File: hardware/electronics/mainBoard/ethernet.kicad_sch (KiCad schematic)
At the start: 34 parts, among them J4 MRJ-5381-01, U4 LAN8742AI

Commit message: assigned net classes
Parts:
- renumbered C39 to C36, C36 to C37, C37 to C38, C38 to C39, R26 to R15, R27 to R16, R28 to R17, R29 to R18, R18 to R19, R22 to R21, R23 to R22, R24 to R23, R15 to R24, R16 to R25, R17 to R26, R19 to R27, R25 to R28, R21 to R29
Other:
- note added: "RMII: 50MHz clock MII: 25MHz clock"
- note added: "Single ended impedance: 50 Ohm Length matching: +/- 1.27mm for RX/RX and TX/TX pairs"

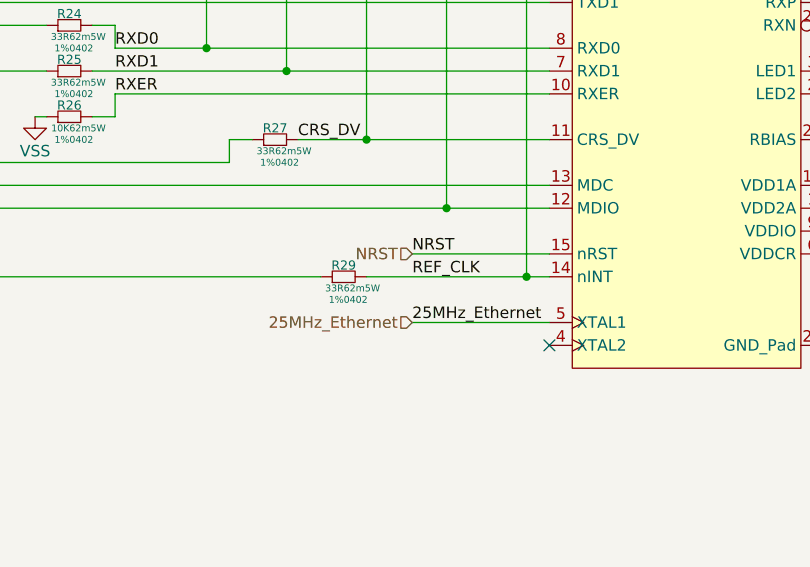
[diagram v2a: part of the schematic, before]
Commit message: fixed net names
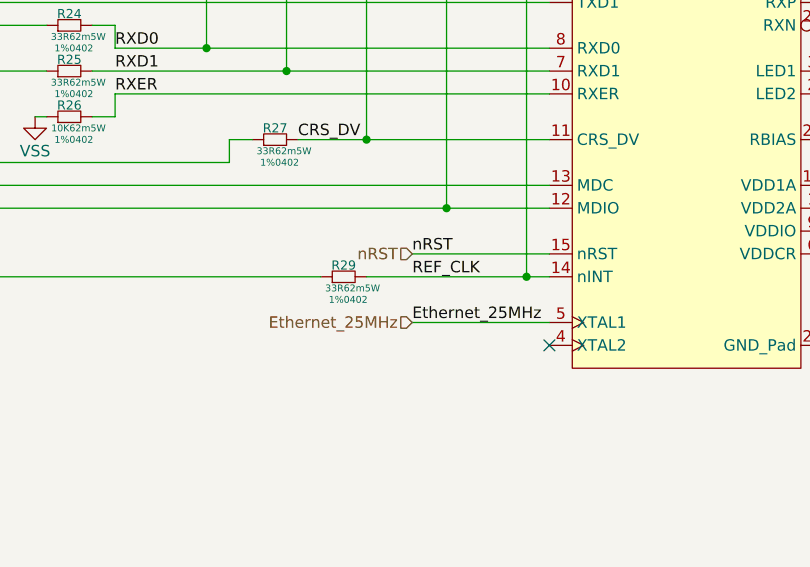
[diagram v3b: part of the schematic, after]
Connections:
- net 25MHz_Ethernet renamed Ethernet_25MHz
- net NRST renamed nRST
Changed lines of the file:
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@@
 		)
 	)
-	(label "25MHz_Ethernet"
+	(label "Ethernet_25MHz"
 		(at 109.22 133.35 0)
 		(effects
@@
 		)
 	)
-	(label "NRST"
+	(label "nRST"
 		(at 109.22 125.73 0)
 		(effects
@@
 		)
 	)
-	(hierarchical_label "25MHz_Ethernet"
+	(hierarchical_label "Ethernet_25MHz"
 		(shape input)
 		(at 109.22 133.35 180)
@@
 		)
 	)
-	(hierarchical_label "NRST"
+	(hierarchical_label "nRST"
 		(shape input)
 		(at 109.22 125.73 180)

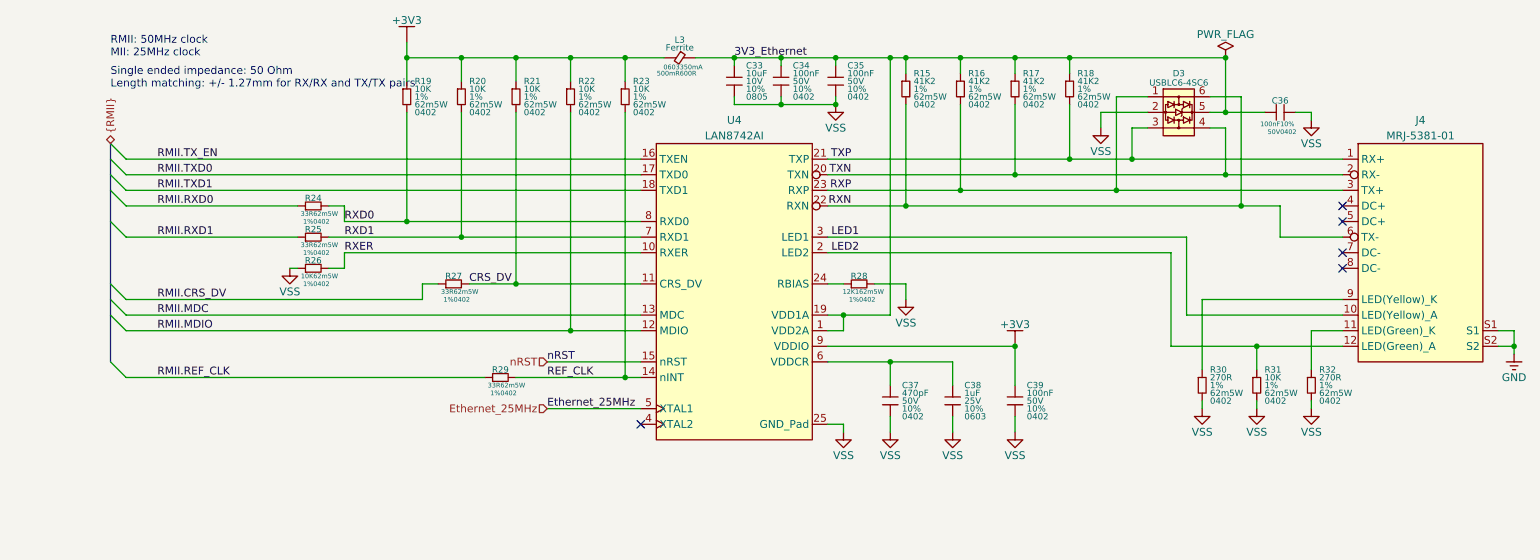
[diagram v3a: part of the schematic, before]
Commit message: fixed net names and added notes
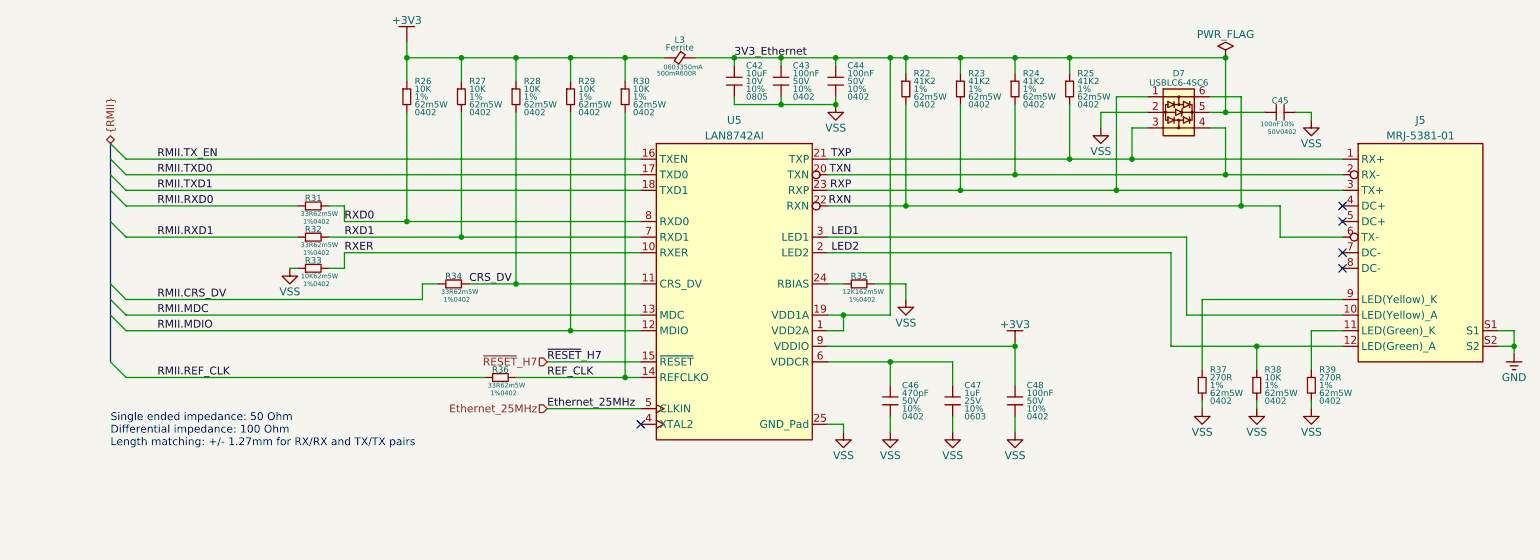
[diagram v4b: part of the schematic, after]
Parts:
- renumbered C33 to C42, C34 to C43, C35 to C44, C36 to C45, C37 to C46, C38 to C47, C39 to C48, D3 to D7, J4 to J5, R15 to R22, R16 to R23, R17 to R24, R18 to R25, R19 to R26, R20 to R27, R21 to R28, R22 to R29, R23 to R30, R24 to R31, R25 to R32, R26 to R33, R27 to R34, R28 to R35, R29 to R36, R30 to R37, R31 to R38, R32 to R39, U4 to U5
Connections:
- net nRST renamed ~{RESET}_H7
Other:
- note added: "Single ended impedance: 50 Ohm Differential impedance: 100 Ohm Length matching: +/- 1.27mm for RX/RX and TX/TX pairs"
- note removed: "RMII: 50MHz clock MII: 25MHz clock"
- note removed: "Single ended impedance: 50 Ohm Length matching: +/- 1.27mm for RX/RX and TX/TX pairs"

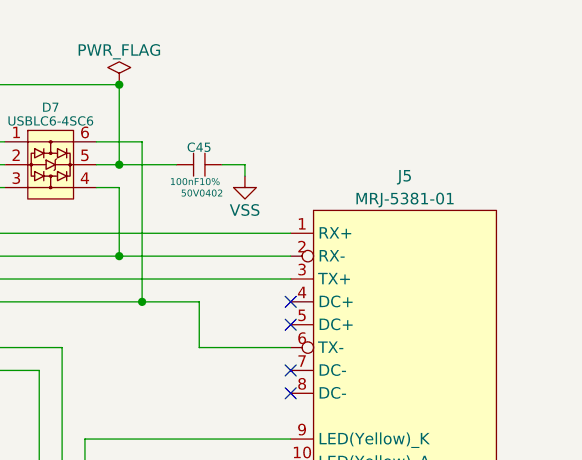
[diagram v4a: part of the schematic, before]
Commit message: renumber references
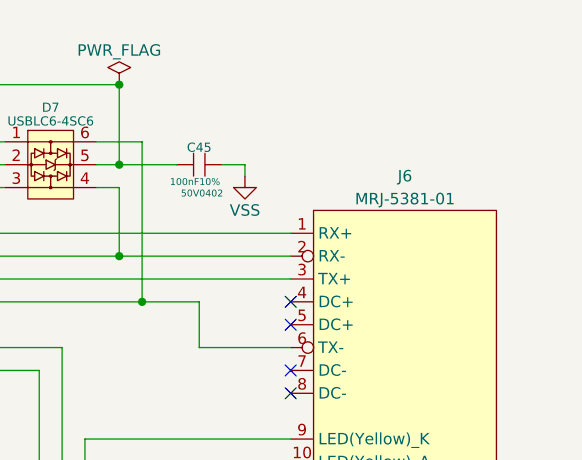
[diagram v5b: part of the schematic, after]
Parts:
- renumbered J5 to J6
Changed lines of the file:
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@@
 		(dnp no)
 		(fields_autoplaced yes)
-		(property "Reference" "#PWR0114"
+		(property "Reference" "#PWR0116"
 			(at 233.68 133.35 0)
 			(effects
@@
 			(project "mainBoard"
 				(path "/be16e32f-2ccf-4272-9ec7-94d5fe7a55e0/7b4a835f-742a-4147-9d08-db52b169b2a7"
-					(reference "#PWR0114")
+					(reference "#PWR0116")
 					(unit 1)
 				)
@@
 		(dnp no)
 		(fields_autoplaced yes)
-		(property "Reference" "#PWR0112"
+		(property "Reference" "#PWR0114"
 			(at 215.9 133.35 0)
 			(effects
@@
 			(project "mainBoard"
 				(path "/be16e32f-2ccf-4272-9ec7-94d5fe7a55e0/7b4a835f-742a-4147-9d08-db52b169b2a7"
-					(reference "#PWR0112")
+					(reference "#PWR0114")
 					(unit 1)
 				)
@@
 		(dnp no)
 		(fields_autoplaced yes)
-		(property "Reference" "#PWR0113"
+		(property "Reference" "#PWR0115"
 			(at 224.79 133.35 0)
 			(effects
@@
 			(project "mainBoard"
 				(path "/be16e32f-2ccf-4272-9ec7-94d5fe7a55e0/7b4a835f-742a-4147-9d08-db52b169b2a7"
-					(reference "#PWR0113")
+					(reference "#PWR0115")
 					(unit 1)
 				)
@@
 		(dnp no)
 		(fields_autoplaced yes)
-		(property "Reference" "J5"
+		(property "Reference" "J6"
 			(at 251.46 86.36 0)
 			(do_not_autoplace yes)
@@
 			(project "mainBoard"
 				(path "/be16e32f-2ccf-4272-9ec7-94d5fe7a55e0/7b4a835f-742a-4147-9d08-db52b169b2a7"
-					(reference "J5")
+					(reference "J6")
 					(unit 1)
 				)
@@
 		(dnp no)
 		(fields_autoplaced yes)
-		(property "Reference" "#PWR0109"
+		(property "Reference" "#PWR0111"
 			(at 167.64 115.57 0)
 			(effects
@@
 			(project "mainBoard"
 				(path "/be16e32f-2ccf-4272-9ec7-94d5fe7a55e0/7b4a835f-742a-4147-9d08-db52b169b2a7"
-					(reference "#PWR0109")
+					(reference "#PWR0111")
 					(unit 1)
 				)
@@
 		(dnp no)
 		(fields_autoplaced yes)
-		(property "Reference" "#PWR0104"
+		(property "Reference" "#PWR0106"
 			(at 86.36 73.66 0)
 			(effects
@@
 			(project "mainBoard"
 				(path "/be16e32f-2ccf-4272-9ec7-94d5fe7a55e0/7b4a835f-742a-4147-9d08-db52b169b2a7"
-					(reference "#PWR0104")
+					(reference "#PWR0106")
 					(unit 1)
 				)
@@
 		(dnp no)
 		(fields_autoplaced yes)
-		(property "Reference" "#PWR0119"
+		(property "Reference" "#PWR0121"
 			(at 30.48 191.77 0)
 			(effects
@@
 			(project "mainBoard"
 				(path "/be16e32f-2ccf-4272-9ec7-94d5fe7a55e0/7b4a835f-742a-4147-9d08-db52b169b2a7"
-					(reference "#PWR0119")
+					(reference "#PWR0121")
 					(unit 1)
 				)
@@
 		(dnp no)
 		(fields_autoplaced yes)
-		(property "Reference" "#PWR0115"
+		(property "Reference" "#PWR0117"
 			(at 157.48 137.16 0)
 			(effects
@@
 			(project "mainBoard"
 				(path "/be16e32f-2ccf-4272-9ec7-94d5fe7a55e0/7b4a835f-742a-4147-9d08-db52b169b2a7"
-					(reference "#PWR0115")
+					(reference "#PWR0117")
 					(unit 1)
 				)
@@
 		(dnp no)
 		(fields_autoplaced yes)
-		(property "Reference" "#PWR0105"
+		(property "Reference" "#PWR0107"
 			(at 156.21 83.82 0)
 			(effects
@@
 			(project "mainBoard"
 				(path "/be16e32f-2ccf-4272-9ec7-94d5fe7a55e0/7b4a835f-742a-4147-9d08-db52b169b2a7"
-					(reference "#PWR0105")
+					(reference "#PWR0107")
 					(unit 1)
 				)
@@
 		(dnp no)
 		(fields_autoplaced yes)
-		(property "Reference" "#PWR0107"
+		(property "Reference" "#PWR0109"
 			(at 199.39 87.63 0)
 			(effects
@@
 			(project "mainBoard"
 				(path "/be16e32f-2ccf-4272-9ec7-94d5fe7a55e0/7b4a835f-742a-4147-9d08-db52b169b2a7"
-					(reference "#PWR0107")
+					(reference "#PWR0109")
 					(unit 1)
 				)
@@
 		(dnp no)
 		(fields_autoplaced yes)
-		(property "Reference" "#PWR0118"
+		(property "Reference" "#PWR0120"
 			(at 185.42 137.16 0)
 			(effects
@@
 			(project "mainBoard"
 				(path "/be16e32f-2ccf-4272-9ec7-94d5fe7a55e0/7b4a835f-742a-4147-9d08-db52b169b2a7"
-					(reference "#PWR0118")
+					(reference "#PWR0120")
 					(unit 1)
 				)
@@
 		(dnp no)
 		(fields_autoplaced yes)
-		(property "Reference" "#PWR0117"
+		(property "Reference" "#PWR0119"
 			(at 175.26 137.16 0)
 			(effects
@@
 			(project "mainBoard"
 				(path "/be16e32f-2ccf-4272-9ec7-94d5fe7a55e0/7b4a835f-742a-4147-9d08-db52b169b2a7"
-					(reference "#PWR0117")
+					(reference "#PWR0119")
 					(unit 1)
 				)
@@
 		(dnp no)
 		(fields_autoplaced yes)
-		(property "Reference" "#PWR0110"
+		(property "Reference" "#PWR0112"
 			(at 185.42 123.19 0)
 			(effects
@@
 			(project "mainBoard"
 				(path "/be16e32f-2ccf-4272-9ec7-94d5fe7a55e0/7b4a835f-742a-4147-9d08-db52b169b2a7"
-					(reference "#PWR0110")
+					(reference "#PWR0112")
 					(unit 1)
 				)
@@
 		(dnp no)
 		(fields_autoplaced yes)
-		(property "Reference" "#PWR0116"
+		(property "Reference" "#PWR0118"
 			(at 165.1 137.16 0)
 			(effects
@@
 			(project "mainBoard"
 				(path "/be16e32f-2ccf-4272-9ec7-94d5fe7a55e0/7b4a835f-742a-4147-9d08-db52b169b2a7"
-					(reference "#PWR0116")
+					(reference "#PWR0118")
 					(unit 1)
 				)
@@
 		(dnp no)
 		(fields_autoplaced yes)
-		(property "Reference" "#PWR0108"
+		(property "Reference" "#PWR0110"
 			(at 67.31 110.49 0)
 			(effects
@@
 			(project "mainBoard"
 				(path "/be16e32f-2ccf-4272-9ec7-94d5fe7a55e0/7b4a835f-742a-4147-9d08-db52b169b2a7"
-					(reference "#PWR0108")
+					(reference "#PWR0110")
 					(unit 1)
 				)
@@
 		(dnp no)
 		(fields_autoplaced yes)
-		(property "Reference" "#PWR0106"
+		(property "Reference" "#PWR0108"
 			(at 233.68 86.36 0)
 			(effects
@@
 			(project "mainBoard"
 				(path "/be16e32f-2ccf-4272-9ec7-94d5fe7a55e0/7b4a835f-742a-4147-9d08-db52b169b2a7"
-					(reference "#PWR0106")
+					(reference "#PWR0108")
 					(unit 1)
 				)
@@
 		(dnp no)
 		(fields_autoplaced yes)
-		(property "Reference" "#PWR0111"
+		(property "Reference" "#PWR0113"
 			(at 266.7 124.46 0)
 			(effects
@@
 			(project ""
 				(path "/be16e32f-2ccf-4272-9ec7-94d5fe7a55e0/7b4a835f-742a-4147-9d08-db52b169b2a7"
-					(reference "#PWR0111")
+					(reference "#PWR0113")
 					(unit 1)
 				)

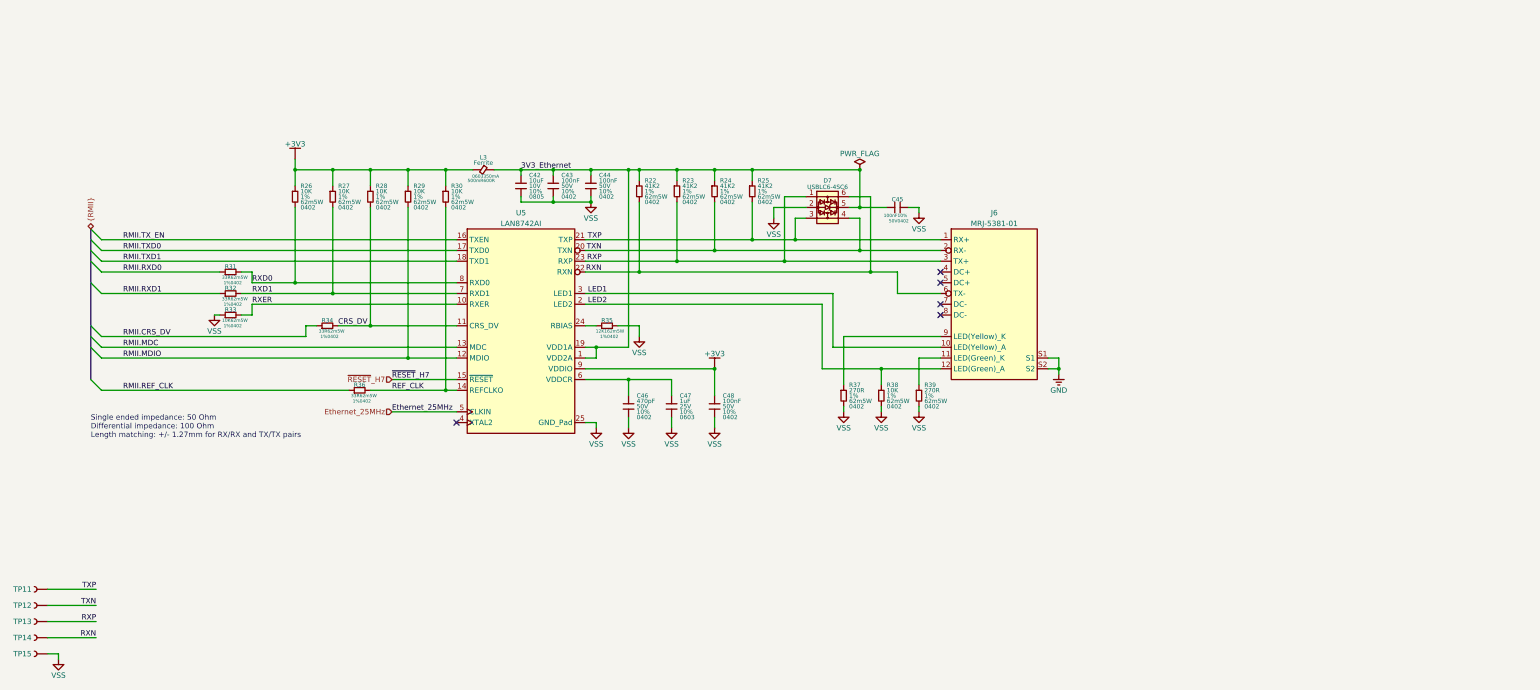
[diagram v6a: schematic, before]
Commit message: added pulse transformer, organized page, and added notes
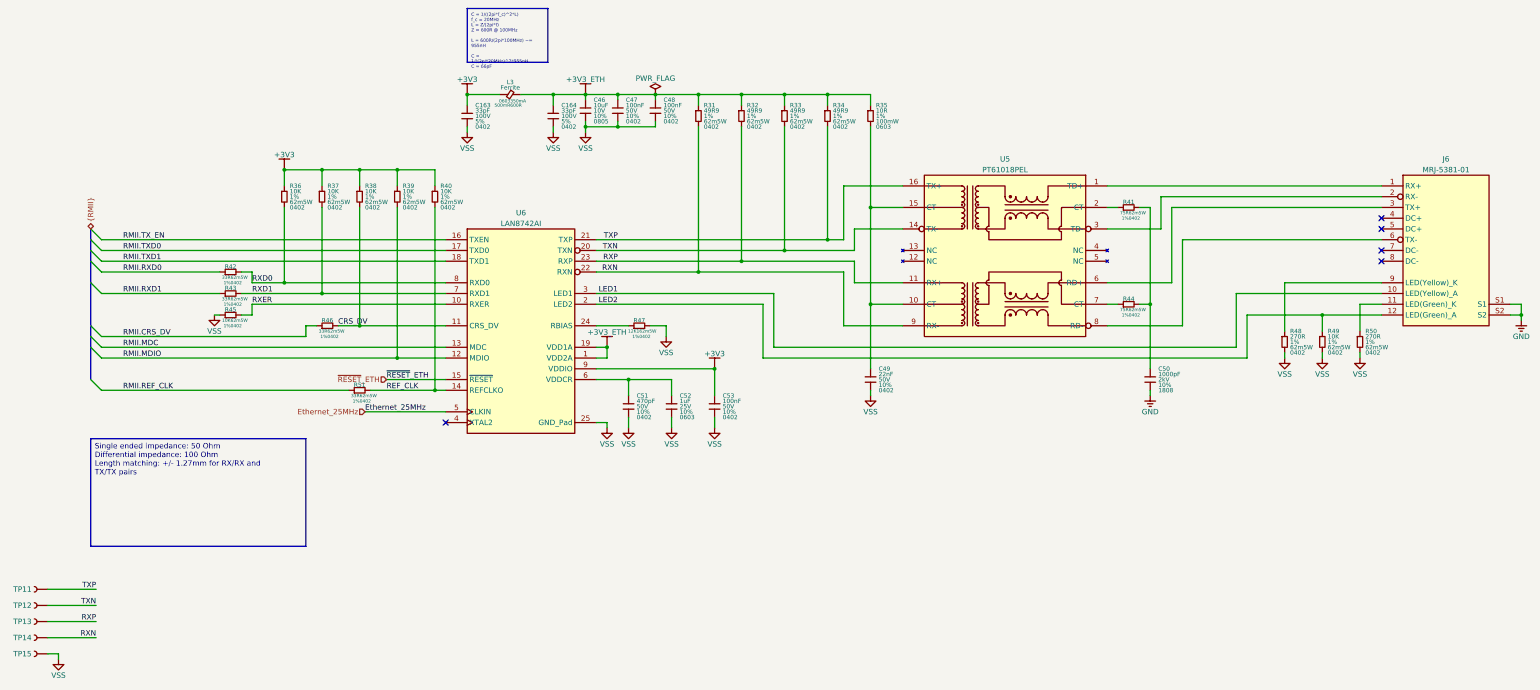
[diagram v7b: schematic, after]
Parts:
- removed C45: 100nF, lib_passives:GCM0402, symbol lib_sch:C_horizontal
- removed D7: USBLC6-4SC6, lib_ICs:SOT2395P280X145-6, symbol lib_sch:D_TVS_2CH_PWR
- removed R22, R23, R24, R25: 41K2, lib_passives:CRCW0402, symbol lib_sch:R
- added C163, C164: 33pF, lib_passives:GCM0402, symbol lib_sch:C
- added C49: 22nF, lib_passives:GCM0402, symbol lib_sch:C
- added C50: 1000pF, lib_passives:GR442, symbol lib_sch:C
- added R31, R32, R33, R34: 49R9, lib_passives:CRCW0402, symbol lib_sch:R
- added R35: 10R, lib_passives:CRCW0603, symbol lib_sch:R
- added R41, R44: 75R, lib_passives:CRCW0402, symbol lib_sch:R_horizontal
- added U5: PT61018PEL, lib_ICs:SOP127P930X565-16, symbol lib_sch:LAN_10/100_Base-T_Pulse_Transformer
- renumbered C42 to C46, C43 to C47, C44 to C48, C46 to C51, C47 to C52, C48 to C53, R26 to R36, R27 to R37, R28 to R38, R29 to R39, R30 to R40, R31 to R42, R32 to R43, R33 to R45, R34 to R46, R35 to R47, R37 to R48, R38 to R49, R39 to R50, R36 to R51, U5 to U6
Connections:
- net +3V3: now also C163.1
- net GND: now also C50.2
- net RXN: now also R31.2, U5.9 (RX-); no longer J6.6 (TX-)
- net RXP: now also R32.2, U5.11 (RX+); no longer J6.3 (TX+)
- net TXN: now also R33.2, U5.14 (TX-); no longer J6.2 (RX-)
- net TXP: now also R34.2, U5.16 (TX+); no longer J6.1 (RX+)
- net VSS: now also C163.2, C164.2, C49.2
- net 3V3_Ethernet renamed +3V3_ETH
- net +3V3_ETH: now also C164.1, R31.1, R32.1, R33.1, R34.1, R35.1
- net ~{RESET}_H7 renamed ~{RESET}_ETH
- new net: J6.1 (RX+), U5.1 (TD+)
- new net: C49.1, R35.2, U5.10 (CT), U5.15 (CT)
- new net: R41.1, U5.2 (CT)
- new net: J6.2 (RX-), U5.3 (TD-)
- new net: J6.3 (TX+), U5.6 (RD+)
- new net: R44.1, U5.7 (CT)
- new net: J6.6 (TX-), U5.8 (RD-)
- new net: C50.1, R41.2, R44.2
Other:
- note removed: "Single ended impedance: 50 Ohm Differential impedance: 100 Ohm Length matching: +/- 1.27mm for RX/RX and TX/TX pairs"
- title: Ethernet -> Awohali Ethernet
- moved on the sheet: C46, C47, C48, J6, L3, R36, R37, R38, R39, R40, R47, R48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
